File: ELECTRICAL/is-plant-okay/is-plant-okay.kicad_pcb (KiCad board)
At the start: 2 copper layers, 43 parts, among them J1 TSW-104-07-F-D, J5 PPTC111LFBN-RC, J6 10129381-918001BLF, J7 USB4085-GF-A_REVB, U6 USBLC6-2SC6, U7 MCP73871-2CCI_ML, U8 MIC5365-3.3YMT-TZ, U9 Value

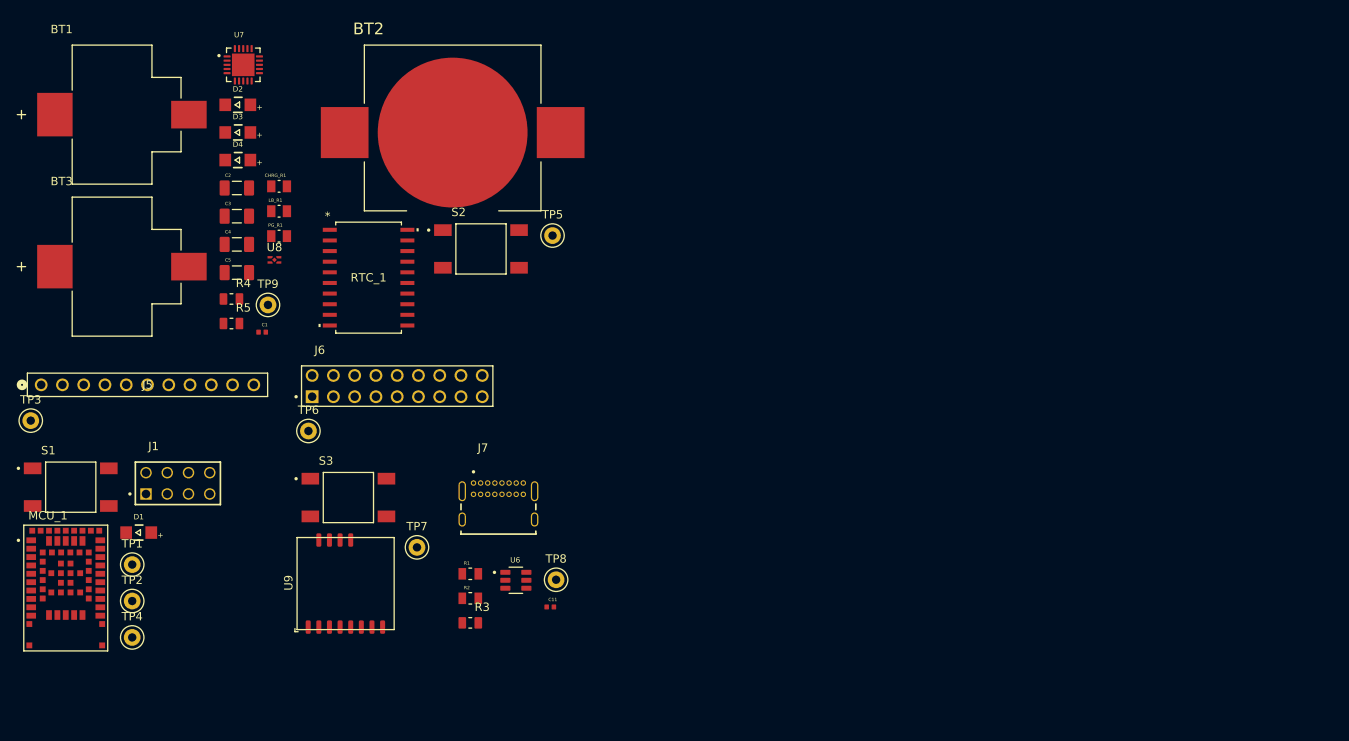
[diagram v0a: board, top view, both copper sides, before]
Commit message: feat: add definitions to pcb
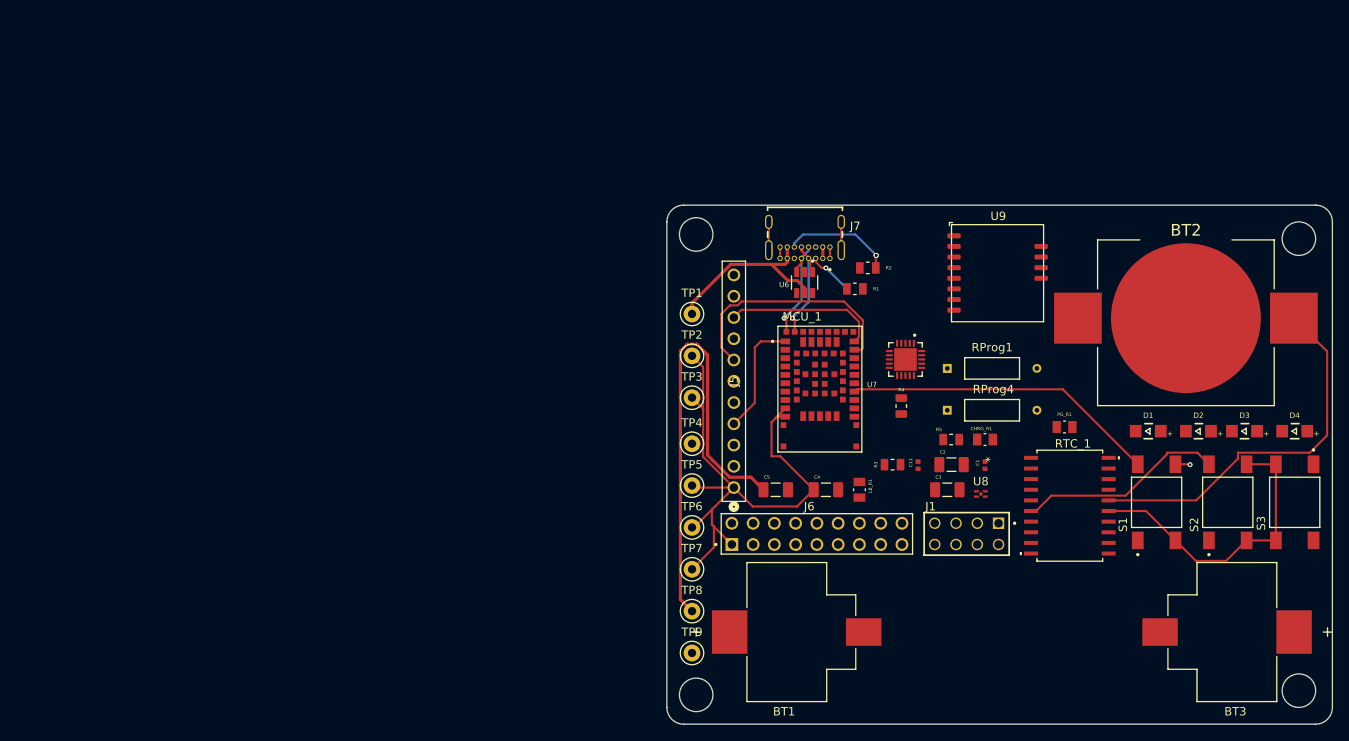
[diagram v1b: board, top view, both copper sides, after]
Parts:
- added RProg1: 10k, is-plant-okay-foot:RES_ZOR25_6P3X2P3_YAG, F.Cu at (171.0, 98.5)
- added RProg4: 0, is-plant-okay-foot:RES_ZOR25_6P3X2P3_YAG, F.Cu at (171.0, 103.5)
- moved BT3 139.1 mm to (204.4, 130.0), turned to 180 degrees
- moved D4 130.3 mm to (212.5, 106.0)
- moved S1 129.7 mm to (196.0, 114.5), turned to 90 degrees
- moved D3 125.4 mm to (206.5, 106.0)
- moved D1 121.2 mm to (195.0, 106.0)
- moved D2 121.2 mm to (201.0, 106.0)
- moved S3 113.1 mm to (212.5, 114.5), turned to -90 degrees
- moved BT1 101.6 mm to (153.0, 130.0)
- moved PG_R1 96.6 mm to (185.0, 105.5), turned to 180 degrees
- moved J1 94.4 mm to (173.3, 118.3), turned to 180 degrees
- moved S2 94.2 mm to (204.5, 114.5), turned to 90 degrees
- moved MCU_1 93.2 mm to (155.8, 101.0)
- moved U9 91.9 mm to (171.5, 81.3), turned to -90 degrees
- moved C2 91.5 mm to (171.5, 110.0)
- moved C3 90.9 mm to (171.0, 113.0)
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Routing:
- net /5V: track 0.00 -> 79.7 mm
- net /3.3V: track 0.00 -> 69.3 mm
- net Net-(RTC_1-VBAT): track 0.00 -> 45.4 mm
- net GND: track 0.00 -> 40.5 mm, vias 0 -> 1
- net Net-(MCU_1-~{RESET}): track 0.00 -> 37.7 mm
- net /TFT_CS: track 0.00 -> 29.0 mm
- net Net-(RTC_1-*RST): track 0.00 -> 24.8 mm
- net /TFT_DC: track 0.00 -> 18.5 mm
- net /LORA_SCLK: track 0.00 -> 14.1 mm
- net /DATA_NEG: track 0.00 -> 13.4 mm, vias 0 -> 1
- net Net-(J7-CC2): track 0.00 -> 13.2 mm, vias 0 -> 2
- net /DATA_POS: track 0.00 -> 13.2 mm, vias 0 -> 1
- net Net-(J7-SHELL): track 0.00 -> 6.76 mm
- net Net-(J7-CC1): track 0.00 -> 5.48 mm, vias 0 -> 1
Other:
- board outline added: 79.5 x 62 mm
